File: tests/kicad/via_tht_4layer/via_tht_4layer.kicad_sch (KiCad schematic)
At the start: 4 parts, among them J1 VSRC

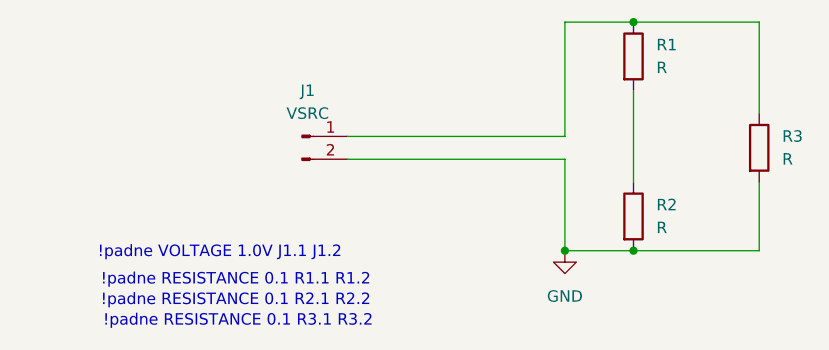
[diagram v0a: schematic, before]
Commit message: feat: Richer directive syntax
This commit adds support for named directive parameters. No more
guessing which parameter is the positive terminal positive and which is the
negative terminal!
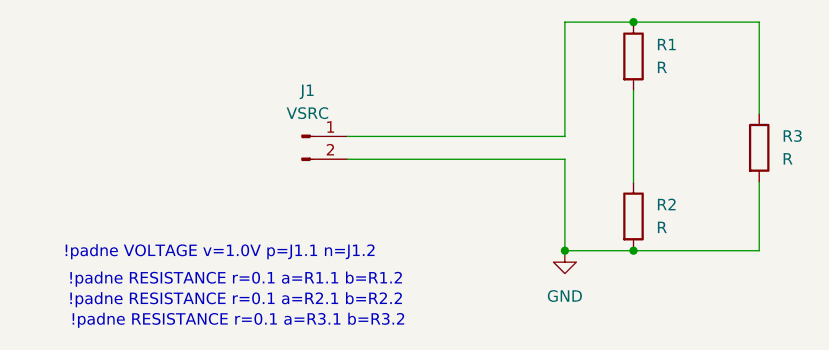
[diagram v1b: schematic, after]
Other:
- note added: "!padne RESISTANCE r=0.1 a=R1.1 b=R1.2"
- note added: "!padne RESISTANCE r=0.1 a=R2.1 b=R2.2"
- note added: "!padne RESISTANCE r=0.1 a=R3.1 b=R3.2"
- note added: "!padne VOLTAGE v=1.0V p=J1.1 n=J1.2"
- note removed: "!padne RESISTANCE 0.1 R1.1 R1.2"
- note removed: "!padne RESISTANCE 0.1 R2.1 R2.2"
- note removed: "!padne RESISTANCE 0.1 R3.1 R3.2"
- note removed: "!padne VOLTAGE 1.0V J1.1 J1.2"
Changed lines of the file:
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@@
 		)
 	)
-	(text "!padne RESISTANCE 0.1 R2.1 R2.2"
+	(text "!padne RESISTANCE r=0.1 a=R2.1 b=R2.2"
 		(exclude_from_sim no)
 		(at 67.564 119.888 0)
@@
 		)
 	)
-	(text "!padne RESISTANCE 0.1 R3.1 R3.2"
+	(text "!padne RESISTANCE r=0.1 a=R3.1 b=R3.2"
 		(exclude_from_sim no)
 		(at 67.818 122.174 0)
@@
 		)
 	)
-	(text "!padne RESISTANCE 0.1 R1.1 R1.2"
+	(text "!padne RESISTANCE r=0.1 a=R1.1 b=R1.2"
 		(exclude_from_sim no)
 		(at 67.564 117.602 0)
@@
 		)
 	)
-	(text "!padne VOLTAGE 1.0V J1.1 J1.2"
+	(text "!padne VOLTAGE v=1.0V p=J1.1 n=J1.2"
 		(exclude_from_sim no)
 		(at 65.786 114.554 0)
